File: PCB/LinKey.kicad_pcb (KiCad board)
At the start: 4 copper layers, 25 x 37.3 mm, 42 parts, among them J2 Conn_01x04, Q1 MMBT2907ALT1G, Q2 CSD25402Q3A, U1 ACPL-214-500E, U2 ESP32-WROOM-32E, U4 TL431DBZ, U5 TPS61022

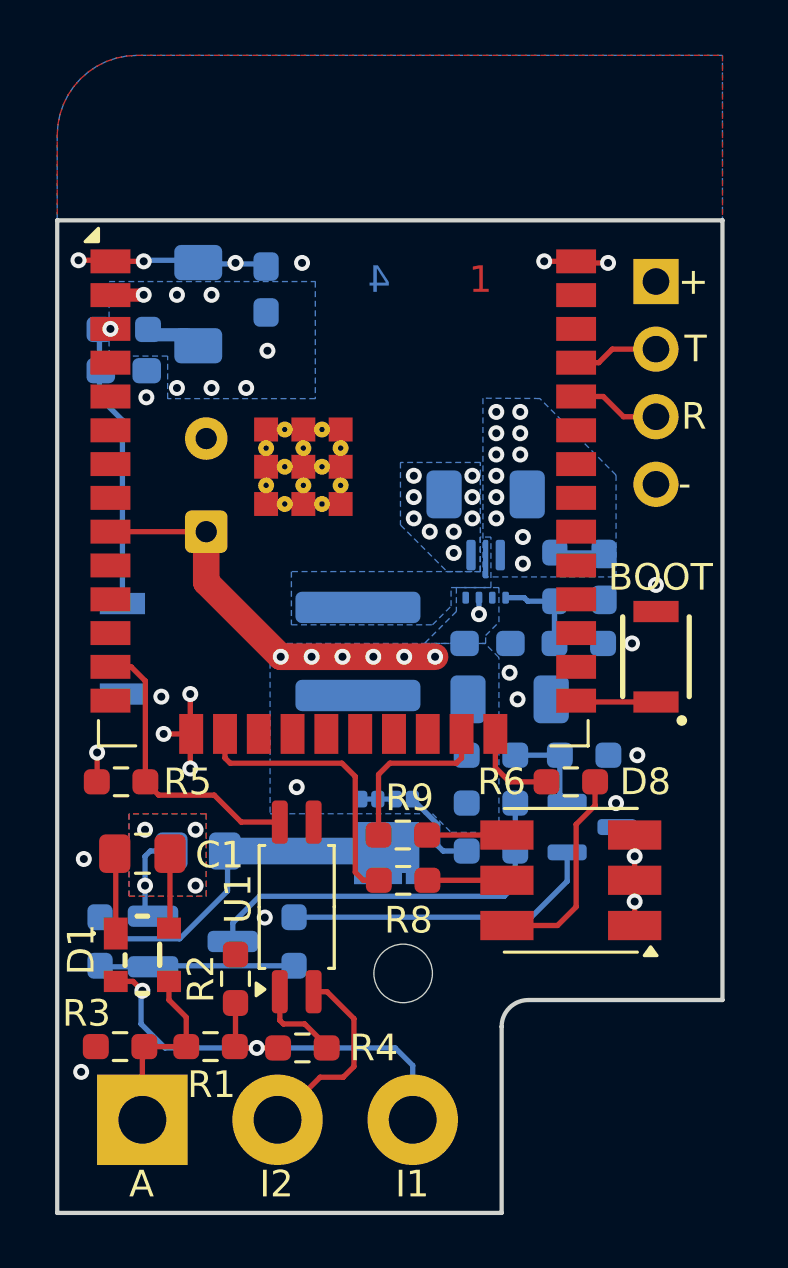
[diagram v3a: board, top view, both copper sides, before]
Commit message: Update PCB v1.1 to better pass DRC
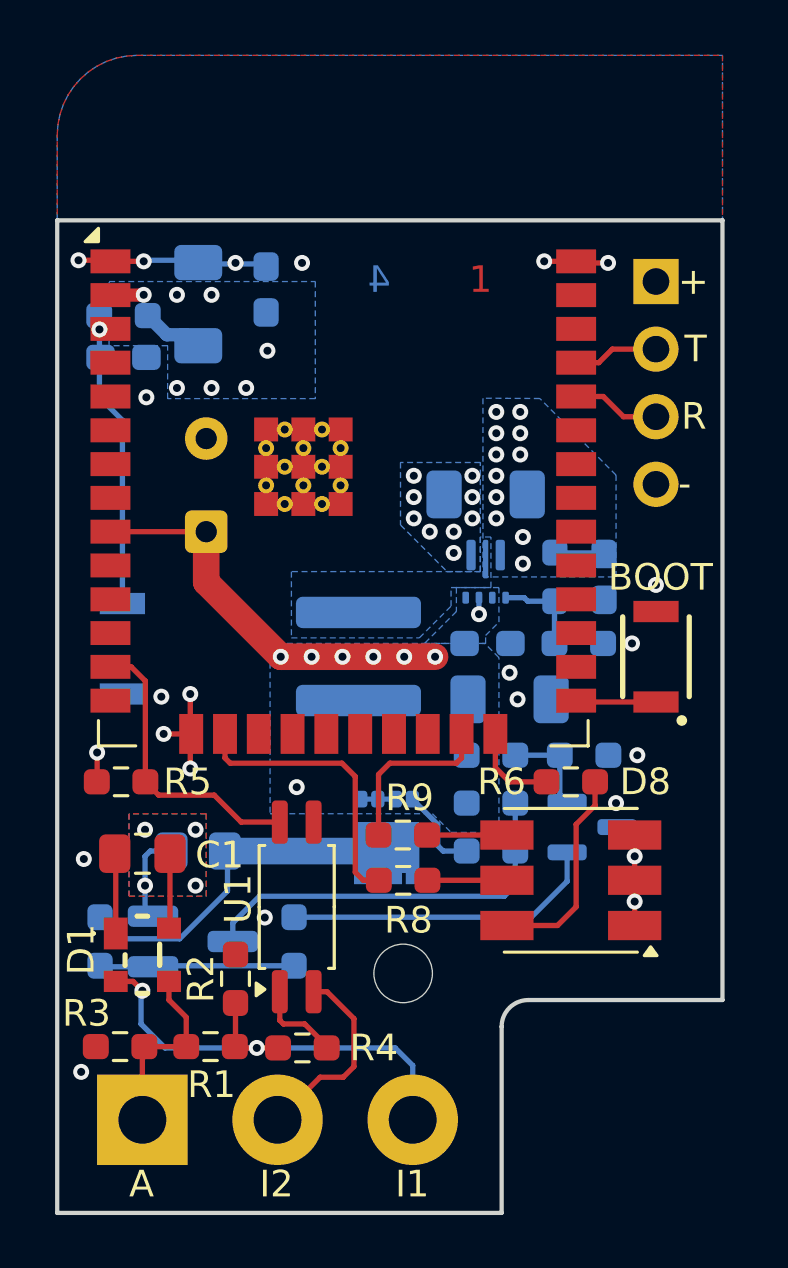
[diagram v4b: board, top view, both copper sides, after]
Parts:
- moved R7 0.52 mm to (143.8, 65.8)
- moved C9 0.50 mm to (143.8, 67.3)
- moved L1 0.19 mm to (152.6, 78.6)
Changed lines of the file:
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@@
 			(at -2.9 1.76)
 			(size 0.6 0.6)
-			(drill 0.2)
+			(drill 0.3)
 			(property pad_prop_heatsink)
 			(layers "*.Cu" "*.Mask")
@@
 			(at -2.9 3.16)
 			(size 0.6 0.6)
-			(drill 0.2)
+			(drill 0.3)
 			(property pad_prop_heatsink)
 			(layers "*.Cu" "*.Mask")
@@
 			(at -2.2 1.06)
 			(size 0.6 0.6)
-			(drill 0.2)
+			(drill 0.3)
 			(property pad_prop_heatsink)
 			(layers "*.Cu" "*.Mask")
@@
 			(at -2.2 2.46)
 			(size 0.6 0.6)
-			(drill 0.2)
+			(drill 0.3)
 			(property pad_prop_heatsink)
 			(layers "*.Cu" "*.Mask")
@@
 			(at -2.2 3.86)
 			(size 0.6 0.6)
-			(drill 0.2)
+			(drill 0.3)
 			(property pad_prop_heatsink)
 			(layers "*.Cu" "*.Mask")
@@
 			(at -1.5 1.76)
 			(size 0.6 0.6)
-			(drill 0.2)
+			(drill 0.3)
 			(property pad_prop_heatsink)
 			(layers "*.Cu" "*.Mask")
@@
 			(at -1.5 3.16)
 			(size 0.6 0.6)
-			(drill 0.2)
+			(drill 0.3)
 			(property pad_prop_heatsink)
 			(layers "*.Cu" "*.Mask")
@@
 			(at -0.8 1.06)
 			(size 0.6 0.6)
-			(drill 0.2)
+			(drill 0.3)
 			(property pad_prop_heatsink)
 			(layers "*.Cu" "*.Mask")
@@
 			(at -0.8 2.46)
 			(size 0.6 0.6)
-			(drill 0.2)
+			(drill 0.3)
 			(property pad_prop_heatsink)
 			(layers "*.Cu" "*.Mask")
@@
 			(at -0.8 3.86)
 			(size 0.6 0.6)
-			(drill 0.2)
+			(drill 0.3)
 			(property pad_prop_heatsink)
 			(layers "*.Cu" "*.Mask")
@@
 			(at -0.1 1.76)
 			(size 0.6 0.6)
-			(drill 0.2)
+			(drill 0.3)
 			(property pad_prop_heatsink)
 			(layers "*.Cu" "*.Mask")
@@
 			(at -0.1 3.16)
 			(size 0.6 0.6)
-			(drill 0.2)
+			(drill 0.3)
 			(property pad_prop_heatsink)
 			(layers "*.Cu" "*.Mask")
@@
 	(footprint "Capacitor_SMD:C_0603_1608Metric_Pad1.08x0.95mm_HandSolder"
 		(layer "B.Cu")
-		(at 143.8 67.85)
+		(at 143.79 67.35)
 		(descr "Capacitor SMD 0603 (1608 Metric), square (rectangular) end terminal, IPC-7351 nominal with elongated pad for handsoldering. (Body size source: IPC-SM-782 page 76, https://www.pcb-3d.com/wordpress/wp-content/uploads/ipc-sm-782a_amendment_1_and_2.pdf), generated with kicad-footprint-generator")
 		(tags "capacitor handsolder")
@@
 	(footprint "Inductor_SMD:L_Coilcraft_XAL5030-XXX"
 		(layer "B.Cu")
-		(at 152.6 78.4 90)
+		(at 152.62 78.59 90)
 		(descr "Inductor, Coilcraft, XAL5030-XXX, 5.48x5.68x3.1mm, (https://www.coilcraft.com/getmedia/49bc46c8-4b2c-45b9-9b6c-2eaa235ea698/xal50xx.pdf), generated with kicad-footprint-generator gen_inductor.py")
 		(tags "xal")
@@
 		(tags "SOT TO_SOT_SMD")
 		(property "Reference" "U4"
-			(at -0.1 2.5 90)
+			(at -0.1 2.5 180)
 			(layer "B.SilkS")
 			(effects
@@
 		(tags "resistor handsolder")
 		(property "Reference" "R12"
-			(at 0 4 90)
+			(at 0 4 180)
 			(layer "B.SilkS")
 			(effects
@@
 	(footprint "Resistor_SMD:R_0603_1608Metric_Pad0.98x0.95mm_HandSolder"
 		(layer "B.Cu")
-		(at 143.8 66.3 180)
+		(at 143.79 65.78 180)
 		(descr "Resistor SMD 0603 (1608 Metric), square (rectangular) end terminal, IPC-7351 nominal with elongated pad for handsoldering. (Body size source: IPC-SM-782 page 72, https://www.pcb-3d.com/wordpress/wp-content/uploads/ipc-sm-782a_amendment_1_and_2.pdf), generated with kicad-footprint-generator")
 		(tags "resistor handsolder")
@@
 	)
 	(segment
+		(start 145.4225 66.5)
+		(end 146.1875 66.5)
+		(width 0.5)
+		(layer "B.Cu")
+		(net 9)
+	)
+	(segment
 		(start 161.6425 74.7)
 		(end 160.2075 74.7)
@@
 	)
 	(segment
-		(start 146.1875 66.5)
-		(end 146.6 66.9125)
-		(width 0.2)
+		(start 144.7025 65.78)
+		(end 145.4225 66.5)
+		(width 0.5)
 		(layer "B.Cu")
 		(net 9)
 	)
 	(segment
-		(start 144.7125 66.3)
-		(end 144.9125 66.5)
+		(start 146.1875 66.5)
+		(end 146.6 66.9125)
 		(width 0.2)
 		(layer "B.Cu")
@@
 	)
 	(segment
-		(start 144.9125 66.5)
-		(end 146.1875 66.5)
-		(width 0.5)
-		(layer "B.Cu")
-		(net 9)
-	)
-	(segment
 		(start 163.4 64.32)
 		(end 163.38 64.3)
@@
 	)
 	(via
-		(at 143.3 66.28)
+		(at 142.8875 66.3)
 		(size 0.6)
 		(drill 0.3)
@@
 		(filled_areas_thickness no)
 		(fill yes
-			(thermal_gap 0.5)
-			(thermal_bridge_width 0.5)
+			(thermal_gap 0.2)
+			(thermal_bridge_width 0.2)
 		)
 		(polygon
 			(pts
-				(xy 145.45 68.9) (xy 145.45 67.3) (xy 143.25 67.3) (xy 143.25 64.5) (xy 151 64.5) (xy 151 68.9)
+				(xy 145.45 68.9) (xy 145.45 66.91) (xy 143.25 66.91) (xy 143.25 64.5) (xy 151 64.5) (xy 151 68.9)
 			)
 		)
@@
 		(polygon
 			(pts
-				(xy 157.6 74.1) (xy 157.2 74.1) (xy 157.2 75.4) (xy 150.1 75.4) (xy 150.1 77.4) (xy 155.4 77.4)
+				(xy 157.6 74.1) (xy 157.2 74.1) (xy 157.2 75.4) (xy 150.1 75.4) (xy 150.1 77.89) (xy 154.91 77.89)
 				(xy 156.1 76.7) (xy 156.1 76) (xy 157.6 76)
 			)

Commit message: refactor(pcb): derive PCB version from git tag pcb-v*
- CI computes version via 'git describe --tags --match pcb-v*' and
  injects it into text_variables.PCB_VERSION in LinKey.kicad_pro before
  running the jobset, so silkscreen ${PCB_VERSION} reflects the build
- fetch-depth: 0 on checkout so describe sees tags
- Artifact name LinKey-pcb-<version>-fab (e.g. v1.0, or v1.0-N-gSHA off-tag)
- Local kicad_pro pins PCB_VERSION to UNCONTROLLED to flag manual exports
- Silkscreen text switched from literal v1.1 to \${PCB_VERSION}
- Rename DRC artifact to LinKey-drc for consistency
- Document the design in PCB/README; add .github/RELEASE_TEMPLATE.md
  (PCB row sources from pcb-vX.Y tag, not project file)
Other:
- board text added: "Linkey ${PCB_VERSION}"
- board text removed: "Linkey ESP32 02.2026 v1.1"
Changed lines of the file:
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@@
 		)
 	)
+	(property "PCB_VERSION" "UNCONTROLLED")
 	(net 0 "")
 	(net 1 "GND")
@@
 		(tags "capacitor handsolder")
 		(property "Reference" "C8"
-			(at -2.45 0 0)
+			(at -1.15 1.81 0)
 			(layer "B.SilkS")
 			(effects
@@
 		(tags "CP Radial series Radial pin pitch 3.50mm diameter 8mm height 12mm Electrolytic Capacitor")
 		(property "Reference" "C2"
-			(at 4.85 4.65 180)
+			(at 3.65 5 180)
 			(layer "B.SilkS")
 			(effects
@@
 	)
 	(gr_line
-		(start 161 79.1)
-		(end 160.8 78.9)
-		(stroke
-			(width 0.1)
-			(type default)
-		)
-		(layer "B.SilkS")
-	)
-	(gr_line
 		(start 157.7 78.9)
 		(end 157.47 78.61)
@@
 	)
 	(gr_line
-		(start 141.3 62.2)
-		(end 166.3 62.2)
+		(start 161 79.1)
+		(end 160.8 78.9)
 		(stroke
-			(width 0.16)
-			(type solid)
+			(width 0.1)
+			(type default)
 		)
-		(layer "Edge.Cuts")
+		(layer "B.SilkS")
 	)
 	(gr_line
-		(start 166.3 91.5)
-		(end 159 91.5)
+		(start 141.3 62.2)
+		(end 141.3 99.5)
 		(stroke
 			(width 0.16)
@@
 	(gr_line
 		(start 141.3 62.2)
-		(end 141.3 99.5)
+		(end 166.3 62.2)
 		(stroke
 			(width 0.16)
@@
 	)
 	(gr_line
-		(start 166.3 62.2)
-		(end 166.3 91.5)
+		(start 158 99.5)
+		(end 141.3 99.5)
 		(stroke
 			(width 0.16)
@@
 	)
 	(gr_line
-		(start 158 99.5)
-		(end 141.3 99.5)
+		(start 166.3 62.2)
+		(end 166.3 91.5)
 		(stroke
 			(width 0.16)
@@
 	)
 	(gr_line
-		(start 166.3 56)
-		(end 166.3 91.5)
+		(start 166.3 91.5)
+		(end 159 91.5)
 		(stroke
 			(width 0.16)
 			(type solid)
 		)
-		(layer "User.4")
+		(layer "Edge.Cuts")
 	)
 	(gr_line
@@
 		(layer "User.4")
 	)
-	(gr_text "R"
-		(at 164.75 70.15 0)
+	(gr_line
+		(start 166.3 56)
+		(end 166.3 91.5)
+		(stroke
+			(width 0.16)
+			(type solid)
+		)
+		(layer "User.4")
+	)
+	(gr_text "A"
+		(at 144 99 0)
 		(layer "F.SilkS")
 		(effects
@@
 		)
 	)
-	(gr_text "-"
-		(at 164.630953 72.683333 0)
+	(gr_text "I2"
+		(at 148.9 99 0)
 		(layer "F.SilkS")
 		(effects
@@
 		)
 	)
-	(gr_text "T"
-		(at 164.869048 67.616666 0)
+	(gr_text "-"
+		(at 164.630953 72.683333 0)
 		(layer "F.SilkS")
 		(effects
@@
 		)
 	)
-	(gr_text "I2"
-		(at 148.9 99 0)
+	(gr_text "R"
+		(at 164.75 70.15 0)
 		(layer "F.SilkS")
 		(effects
@@
 		)
 	)
-	(gr_text "A"
-		(at 144 99 0)
+	(gr_text "T"
+		(at 164.869048 67.616666 0)
 		(layer "F.SilkS")
 		(effects
@@
 		)
 	)
-	(gr_text "Linkey ESP32\n02.2026\nv1.1"
-		(at 162.1 70.8 0)
+	(gr_text "Linkey\n${PCB_VERSION}"
+		(at 162.42 65.77 0)
 		(layer "B.SilkS")
 		(effects
@@
 				(thickness 0.15)
 			)
-			(justify left bottom mirror)
+			(justify left top mirror)
 		)
 	)
